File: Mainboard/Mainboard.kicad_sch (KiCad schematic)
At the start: 13 parts, among them J1 5745782-6

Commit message: working mainboard push!
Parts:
- removed C139: 100n, Capacitor_SMD:C_1206_3216Metric_Pad1.42x1.75mm_HandSolder, symbol Device:C_Small
- removed TP1, TP2, TP3, TP4, TP5, TP6, TP7, TP8: TestPoint, TestPoint:TestPoint_Loop_D1.80mm_Drill1.0mm_Beaded, symbol Connector:TestPoint
- added C39: 100n, Capacitor_SMD:C_0805_2012Metric, symbol Device:C
- R30: footprint Resistor_SMD:R_1206_3216Metric_Pad1.42x1.75mm_HandSolder -> Resistor_SMD:R_0805_2012Metric; Mouser Part Number (none) -> 755-SDR10EZPF1204
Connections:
- net GND: now also C39.2
- net at JP12.2, R30.2: now also C39.1
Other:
- sheet StepperDrivers ports: added DIR_1, DIR_2, DIR_3, STEP_1, STEP_2, STEP_3; removed none
- sheet Teensy4.0 ports: added DIR_1, DIR_2, DIR_3, STEP_1, STEP_2, STEP_3; removed none
- note added: "Remove 5v Vusb bridge on back of teesny!"

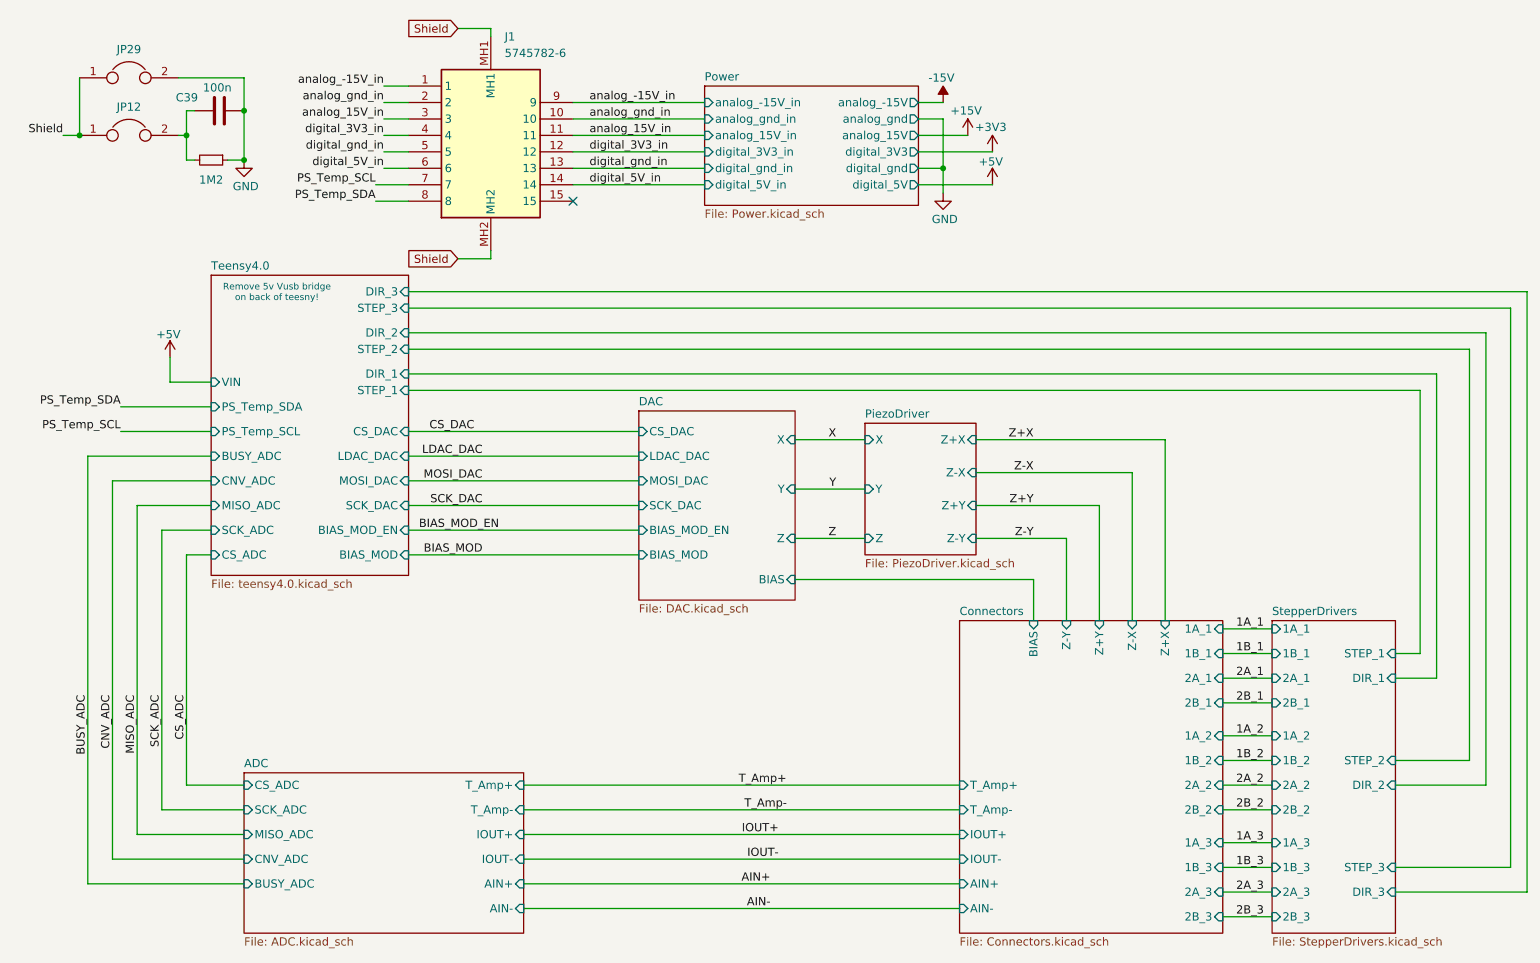
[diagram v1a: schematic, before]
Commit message: mainboard working commits!
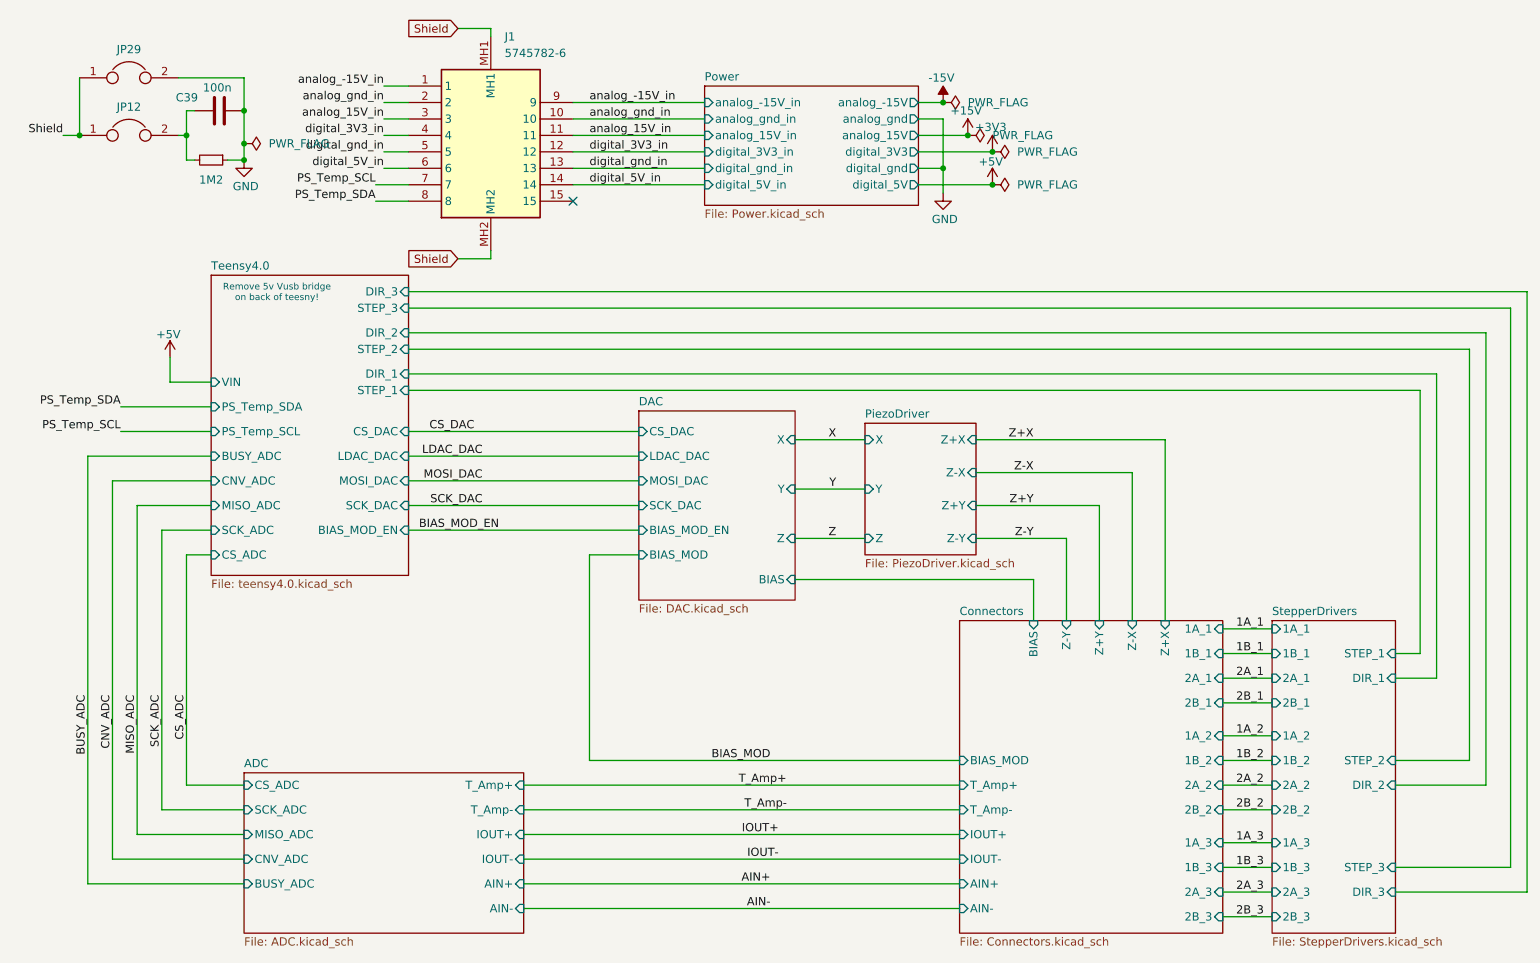
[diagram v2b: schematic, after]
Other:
- sheet Connectors ports: added BIAS_MOD; removed none
- sheet Teensy4.0 ports: added none; removed BIAS_MOD
